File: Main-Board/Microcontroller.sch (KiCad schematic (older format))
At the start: 10 parts

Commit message: Added in microcontroller voltage regulation
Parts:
- added C?: X7R, 100nF 10%, Capacitor_SMD:C_0603_1608Metric_Pad1.05x0.95mm_HandSolder, symbol Device:C
- added C?: 4.7uF 16V, symbol Device:CP
- added C?: X7R, 1uF 10%, Capacitor_SMD:C_0603_1608Metric_Pad1.05x0.95mm_HandSolder, symbol Device:C
- added D?: SS1P3L, symbol Device:D_Schottky
- added D?: LED, symbol Device:LED
- added J?: ICSP, symbol Connector_Generic:Conn_02x03_Odd_Even
- added R?: R, symbol Device:R
- added U?: LM1117-5.0, symbol Regulator_Linear:LM1117-5.0
- added Y?: 16 MHz, symbol Device:Resonator_Small
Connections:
- net labels added: D11, D12, D13, VDD
- wire segments 54 -> 92
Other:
- moved on the sheet: C?, D?, F?, J?, R?, U?

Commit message: Roughed the rest of the microcontroller schematic
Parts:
- added C?: X7R, 100nF 10%, Capacitor_SMD:C_0603_1608Metric_Pad1.05x0.95mm_HandSolder, symbol Device:C
- added C?: 4.7uF 16V, symbol Device:CP
- added C? (x2): X7R, 1uF 10%, Capacitor_SMD:C_0603_1608Metric_Pad1.05x0.95mm_HandSolder, symbol Device:C
- added D?: LED, symbol Device:LED
- added R?: 10 kOhm 5%, symbol Device:R
- added R? (x3): R, symbol Device:R
- added SW?: Reset, symbol Switch:SW_MEC_5G
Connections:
- net labels added: D10, D8, D9
- wire segments 92 -> 121
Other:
- moved on the sheet: U?

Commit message: Filled out majority of microcontroller components and foot prints
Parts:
- removed D? (x2): LED, symbol Device:LED
- removed R? (x2): R, symbol Device:R
- removed Y?: 16 MHz, symbol Device:Resonator_Small
- added C? (x2): X7R, 2pF 2%, Capacitor_SMD:C_0603_1608Metric_Pad1.05x0.95mm_HandSolder, symbol Device:C
- added D?: Orange 1.9V 20mA, LED_SMD:LED_0603_1608Metric_Pad1.05x0.95mm_HandSolder, symbol Device:LED
- added D?: Green 2.2V 20mA, LED_SMD:LED_0603_1608Metric_Pad1.05x0.95mm_HandSolder, symbol Device:LED
- added R? (x2): 200 ohm, Resistor_SMD:R_0603_1608Metric_Pad1.05x0.95mm_HandSolder, symbol Device:R
- added R?: 1 Mohm, Resistor_SMD:R_0603_1608Metric_Pad1.05x0.95mm_HandSolder, symbol Device:R
- added Y?: 16 MHz, Crystal:Resonator-2Pin_W10.0mm_H5.0mm, symbol Device:Crystal
- C?: value 4.7uF 16V -> 4.7uF 16V 20%; footprint (none) -> Capacitor_SMD:C_0603_1608Metric_Pad1.05x0.95mm_HandSolder
- C?: footprint (none) -> Capacitor_SMD:C_0603_1608Metric_Pad1.05x0.95mm_HandSolder
- D?: value LED -> Orange 1.9V 20mA; footprint (none) -> LED_SMD:LED_0603_1608Metric_Pad1.05x0.95mm_HandSolder
- D?: value LED -> Green 2.2V 20mA; footprint (none) -> LED_SMD:LED_0603_1608Metric_Pad1.05x0.95mm_HandSolder
- F?: value Polyfuse_Small -> PTC 15V 500mA; footprint (none) -> Fuse:Fuse_1206_3216Metric_Pad1.42x1.75mm_HandSolder
- J?: footprint (none) -> Connector_USB:USB_Micro-B_Molex-105017-0001; Digi-Key # (none) -> WM1399CT-ND; Digi-Key LinkDigi LinkDigi-Key Link (none) -> https://www.digikey.ca/en/products/detail/molex/1050170001/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; Manufacturer (none) -> Molex; Manufacturer # (none) -> 105017-0001
- J?: footprint (none) -> Connector_PinHeader_2.54mm:PinHeader_2x03_P2.54mm_Vertical
- R?: value R -> 200 ohm; footprint (none) -> Resistor_SMD:R_0603_1608Metric_Pad1.05x0.95mm_HandSolder
- R?: value R -> 140 ohm; footprint (none) -> Resistor_SMD:R_0603_1608Metric_Pad1.05x0.95mm_HandSolder
- R?: footprint (none) -> Resistor_SMD:R_0603_1608Metric_Pad1.05x0.95mm_HandSolder
- R? (x2): value R -> 1 kohm; footprint (none) -> Resistor_SMD:R_0603_1608Metric_Pad1.05x0.95mm_HandSolder
- U?: Digi-Key # (none) -> 768-1007-1-ND; Digi-Key LinkDigi LinkDigi-Key Link (none) -> https://www.digikey.ca/en/products/detail/ftdi-future-techn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; Manufacturer (none) -> FTDI, Future Technology Devices International Ltd; Manufacturer # (none) -> FT232RL-REEL
- U?: footprint (none) -> Package_TO_SOT_SMD:SOT-223; Digi-Key # (none) -> LM1117IMP-5.0/NOPBCT-ND; Digi-Key LinkDigi LinkDigi-Key Link (none) -> https://www.digikey.ca/en/products/detail/texas-instruments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; Manufacturer (none) -> Texas Instruments; Manufacturer # (none) -> LM1117IMP-5.0/NOPB
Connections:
- net labels added: XTAL1, XTAL2
- wire segments 121 -> 131
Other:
- note added: "ICSP"
- note added: "Microcontroller"
- note added: "Power Regulation and Selection"
- note added: "USB Interface"
- moved on the sheet: C?, D?, F?, J?, R?, SW?, U?

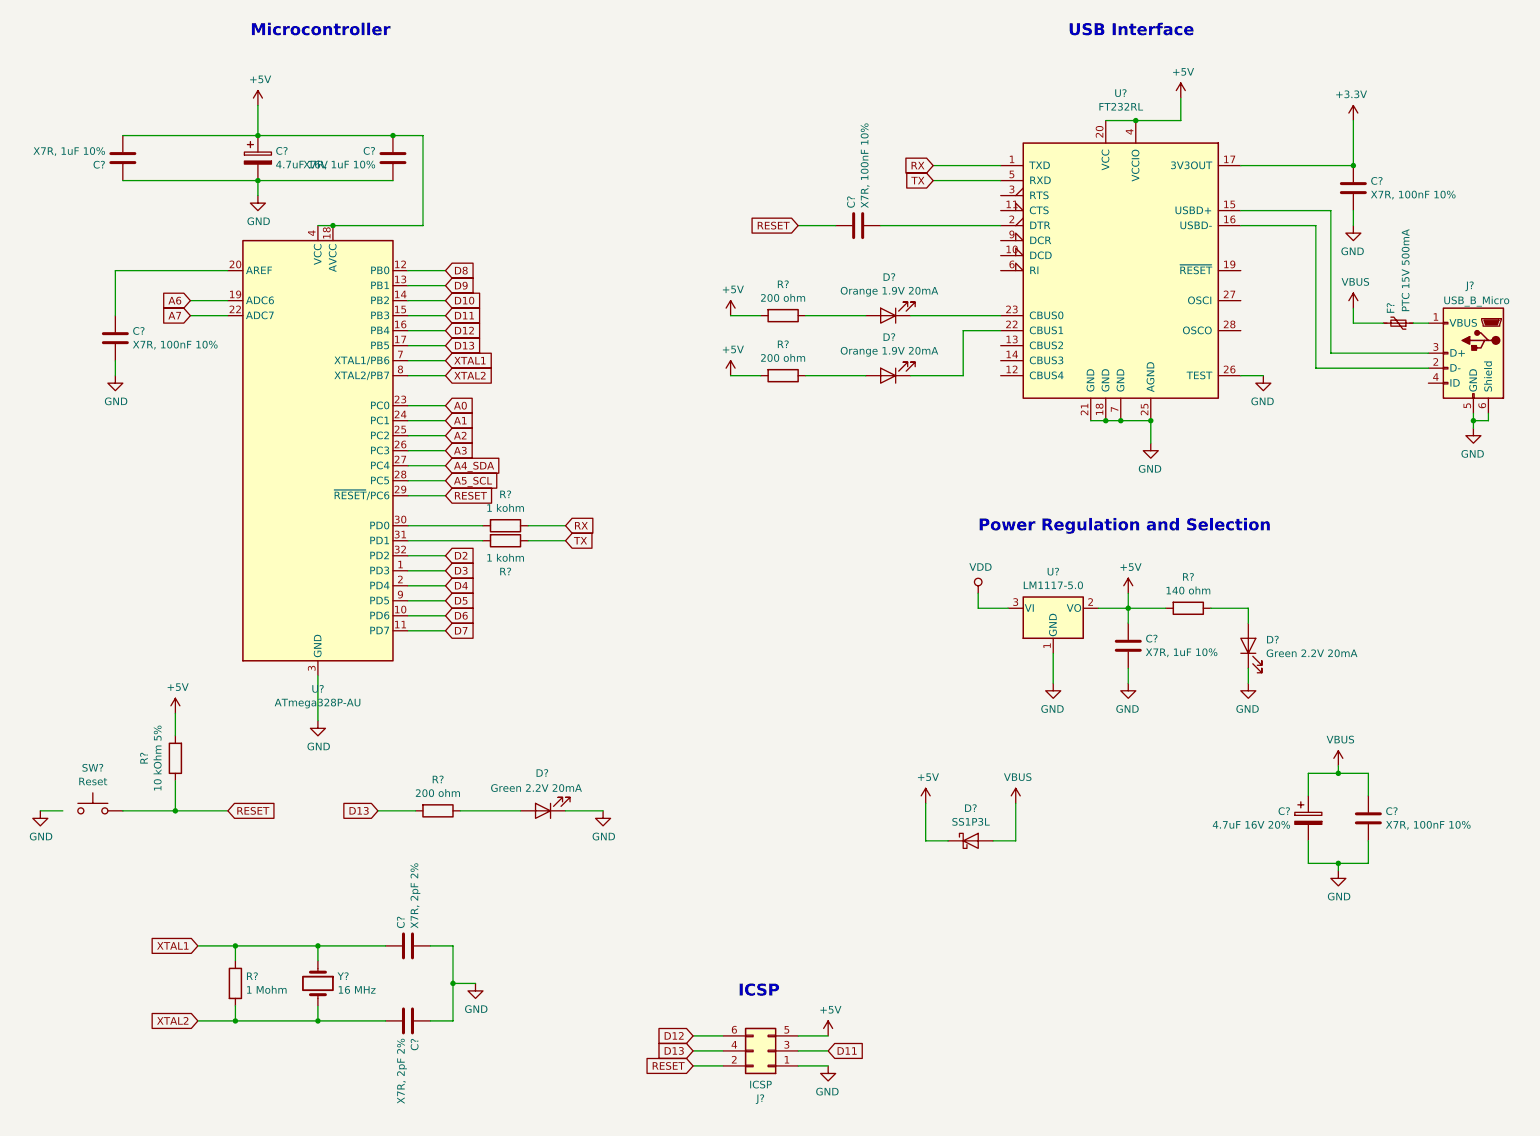
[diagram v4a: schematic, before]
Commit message: Added a few more footprints and component specifics. Created first net list
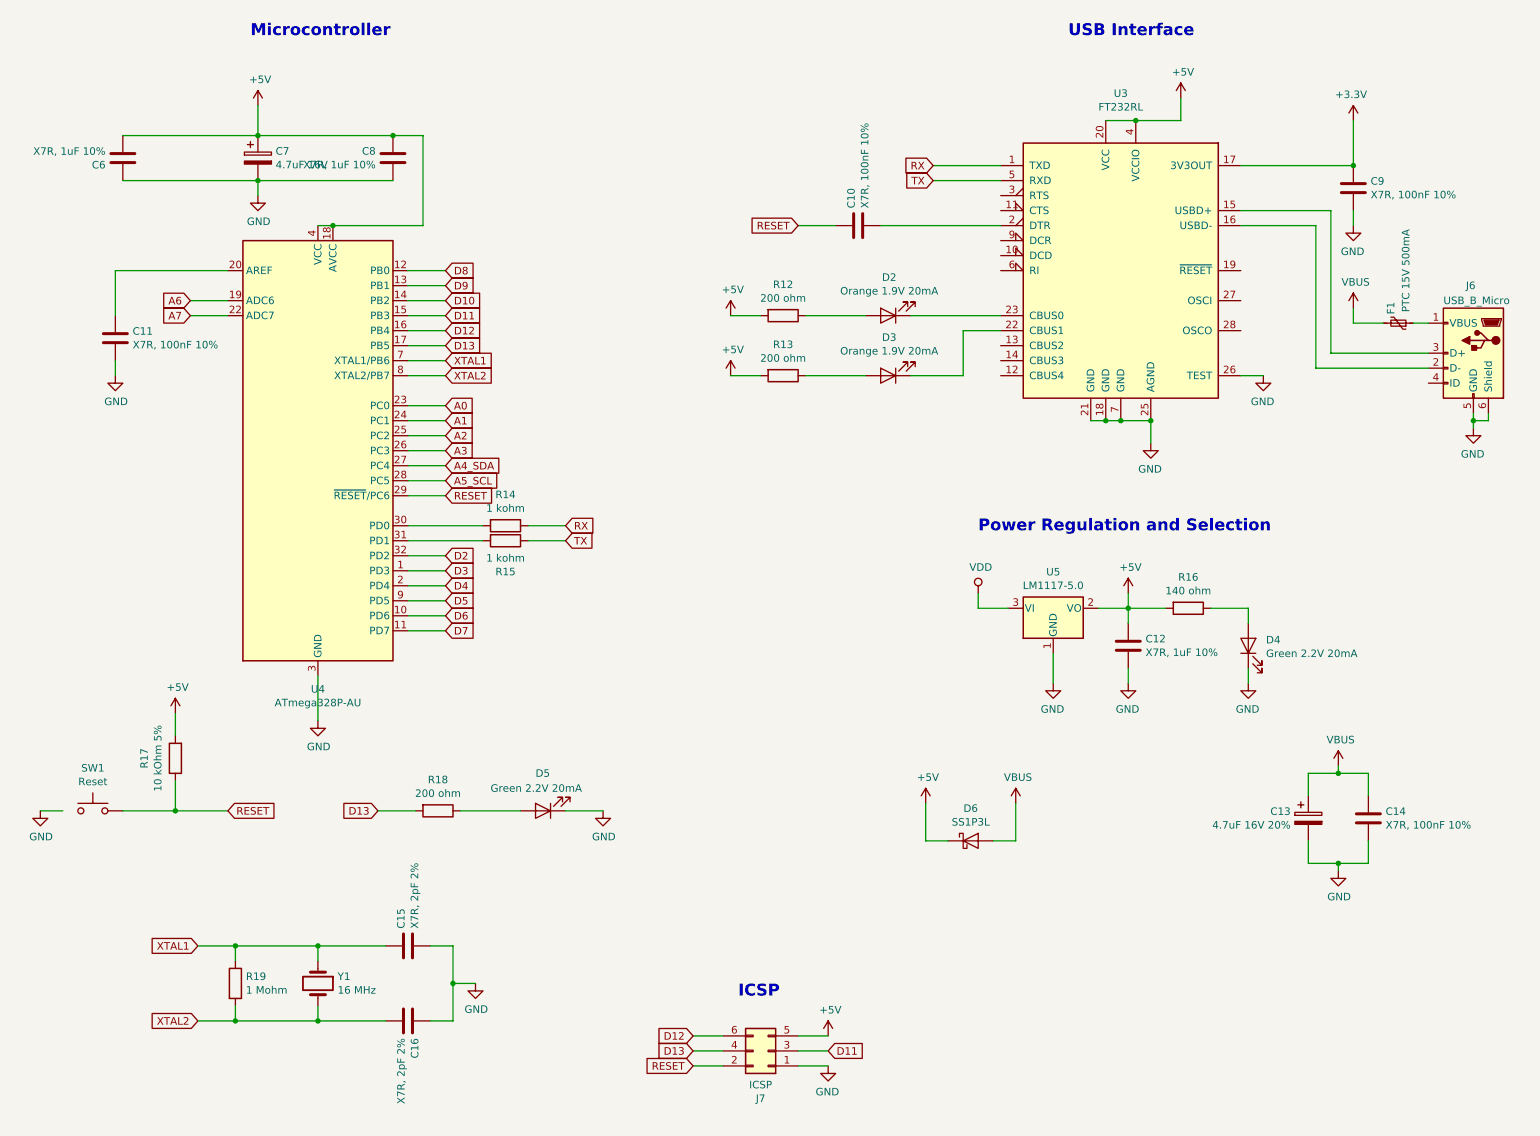
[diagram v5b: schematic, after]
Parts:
- gave numbers to parts that had none: 32

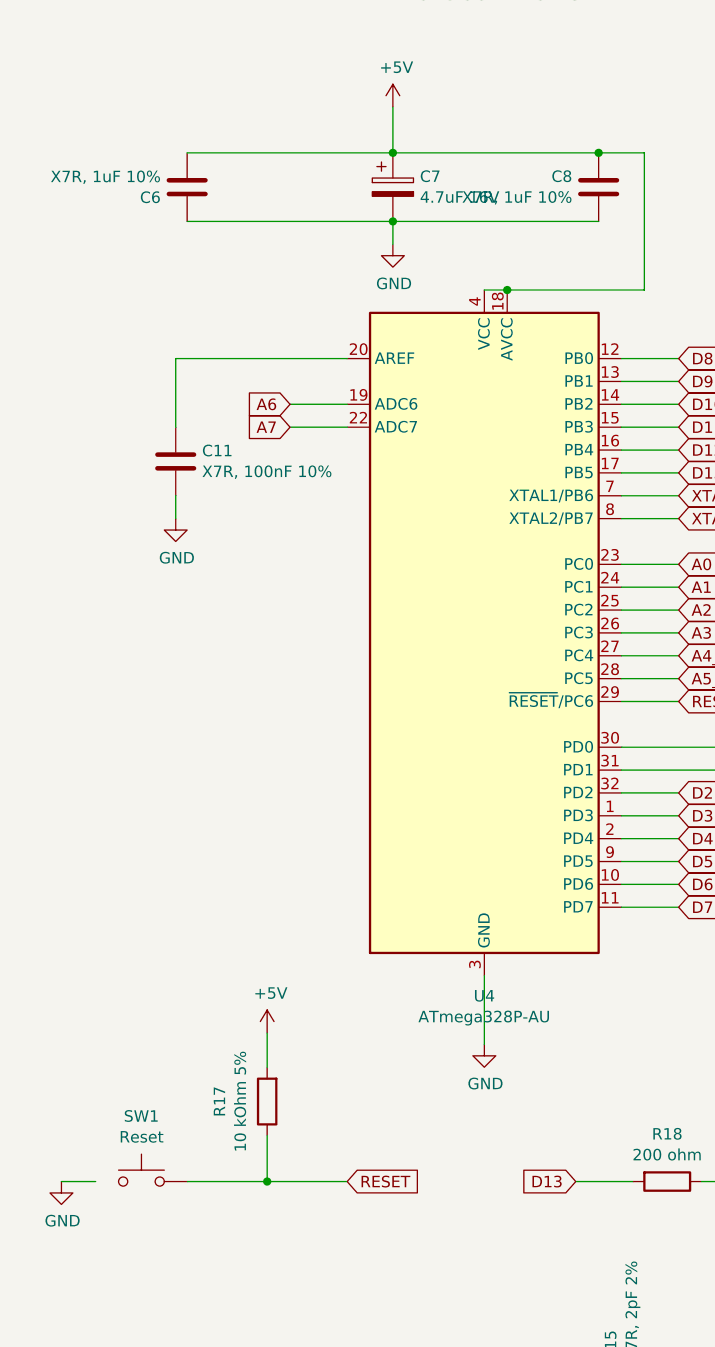
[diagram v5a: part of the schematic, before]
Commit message: Everything is in the schematic. Just need to review board then start the layout. Printed off hard copy
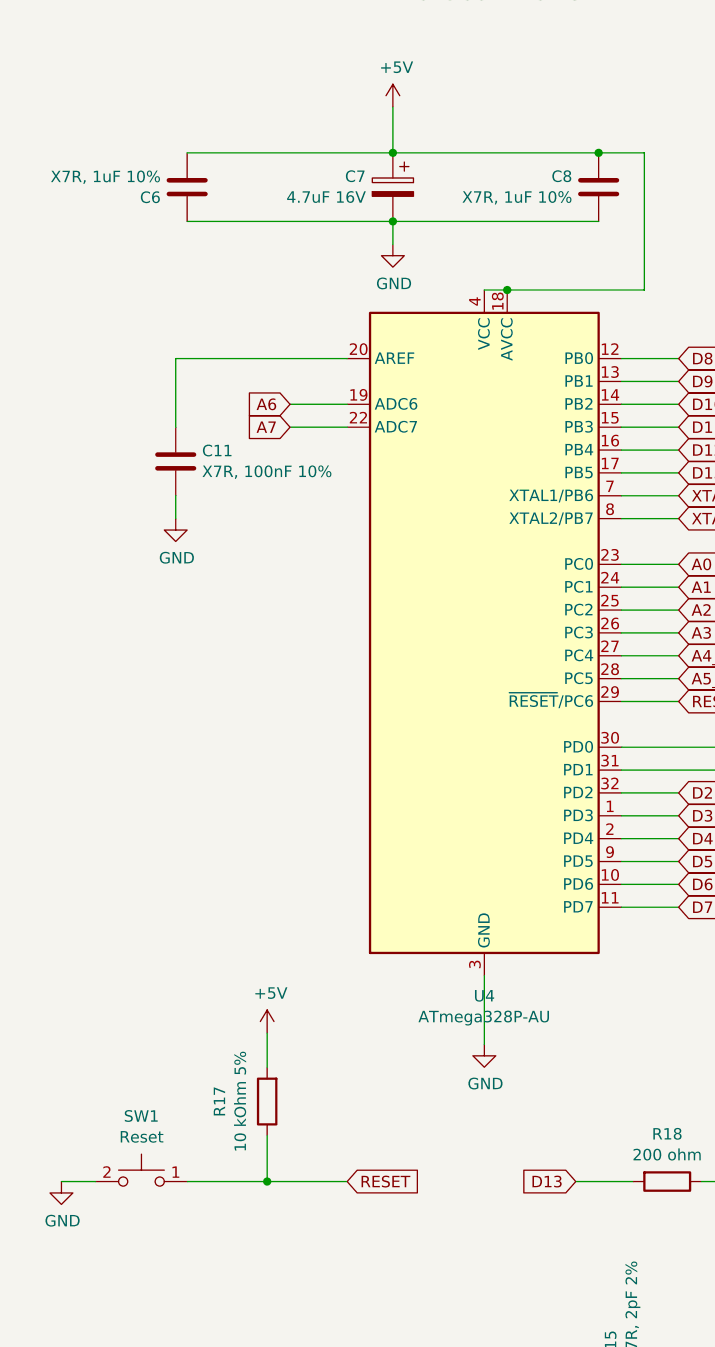
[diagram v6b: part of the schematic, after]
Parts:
- removed SW1: Reset, symbol Switch:SW_MEC_5G
- added SW1: Reset, Custom:Switch, symbol Custom:Push-Switch
- D6: footprint (none) -> Custom:SS1P3L
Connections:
- net GND: now also SW1.2
- net RESET: now also SW1.1
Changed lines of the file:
@@
 F 0 "D6" H 6850 6316 50  0000 C CNN
 F 1 "SS1P3L" H 6850 6225 50  0000 C CNN
-F 2 "" H 6850 6100 50  0001 C CNN
+F 2 "Custom:SS1P3L" H 6850 6100 50  0001 C CNN
 F 3 "~" H 6850 6100 50  0001 C CNN
 	1    6850 6100
@@
 Wire Wire Line
 	5900 7500 5700 7500
-$Comp
-L Switch:SW_MEC_5G SW1
-U 1 1 5FEF10E5
-P 1000 5900
-F 0 "SW1" H 1000 6185 50  0000 C CNN
-F 1 "Reset" H 1000 6094 50  0000 C CNN
-F 2 "" H 1000 6100 50  0001 C CNN
-F 3 "" H 1000 6100 50  0001 C CNN
-	1    1000 5900
-	1    0    0    -1
-$EndComp
 $Comp
 L power:GND #PWR0153
@@
 F 3 "~" H 2100 1550 50  0001 C CNN
 	1    2100 1550
-	1    0    0    -1
+	-1   0    0    -1
 $EndComp
 $Comp
@@
 	1950 7300 1700 7300
 Connection ~ 1950 7300
+$Comp
+L Custom:Push-Switch SW1
+U 1 1 5FDF717A
+P 1000 5850
+F 0 "SW1" H 1000 6085 50  0000 C CNN
+F 1 "Reset" H 1000 5994 50  0000 C CNN
+F 2 "Custom:Switch" H 1000 6100 50  0001 C CNN
+F 3 "" H 1000 6100 50  0001 C CNN
+	1    1000 5850
+	1    0    0    -1
+$EndComp
 $EndSCHEMATC
